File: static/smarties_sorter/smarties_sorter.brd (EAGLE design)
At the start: 170.2 x 100 mm, 17 parts, among them IC1 MEGA8-P, Q1 16Mhz, Q2 IRLZ44Z

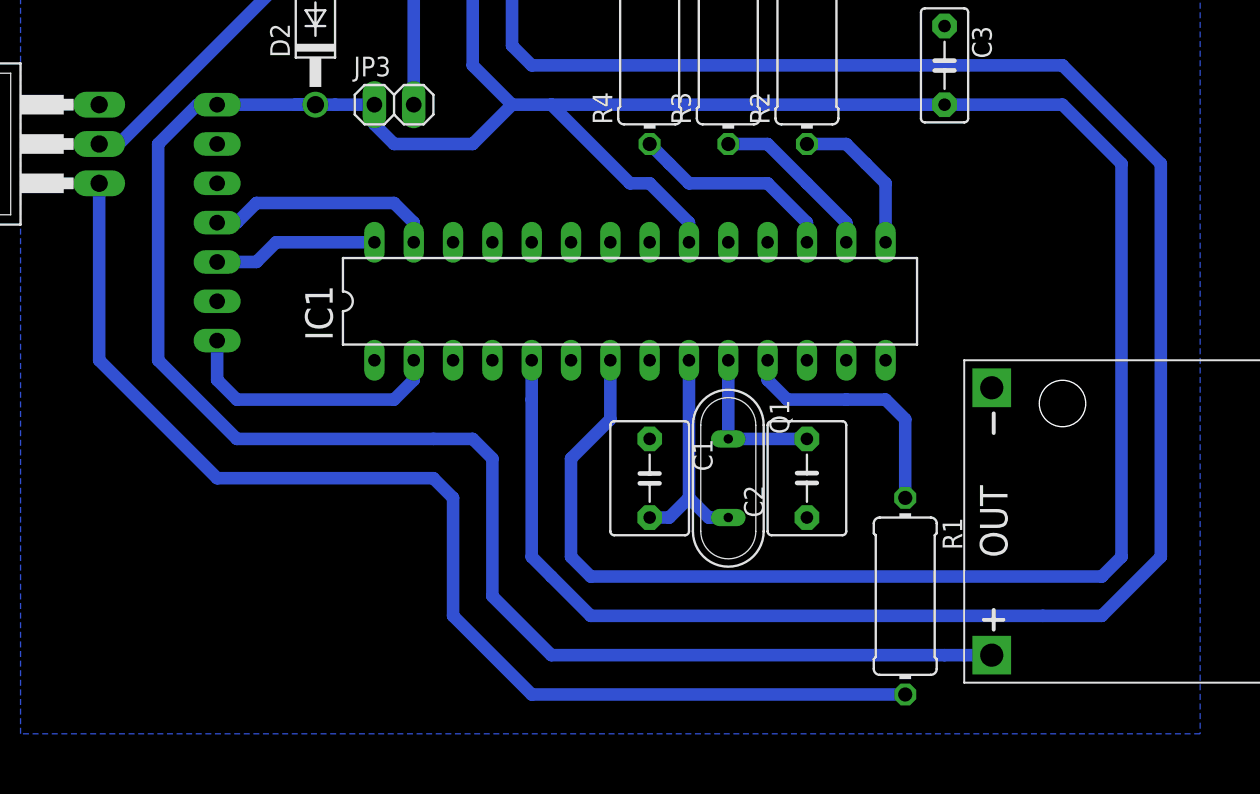
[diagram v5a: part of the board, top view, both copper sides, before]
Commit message: [Smarties_sorter] Change color sensor plug
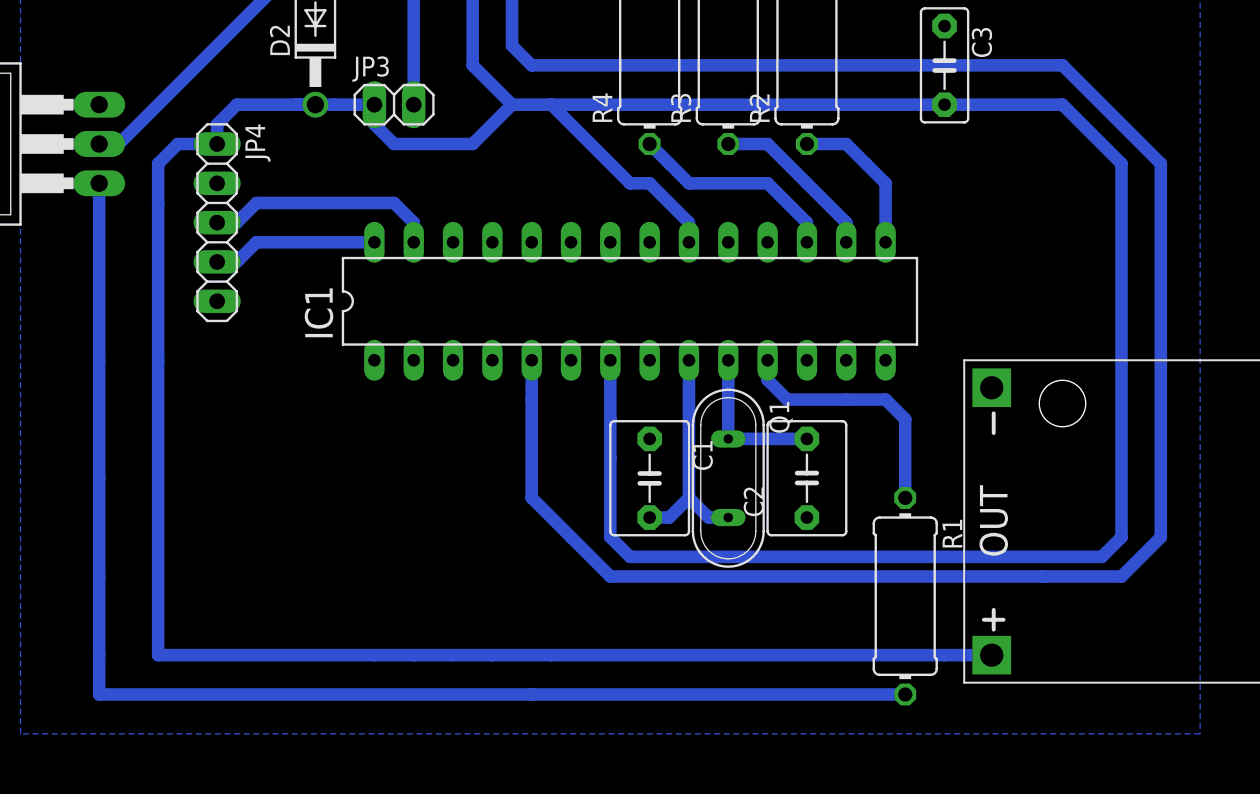
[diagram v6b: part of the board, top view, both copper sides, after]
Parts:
- JP4: device pinhead:1X07 -> pinhead:1X05
- flipped JP4 to the top
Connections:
- removed net N$15: IC1.2, JP4.7
- new net LED_CTRL: IC1.13, JP4.5
- net N$16: now also JP4.4; no longer JP4.5
- net N$17: now also JP4.3; no longer JP4.4
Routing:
- net N$15: track 17.6 -> 0.00 mm
- net N$8: track 76.9 -> 85.1 mm
- net N$6: track 135.9 -> 130.8 mm
- net 5V: track 254.0 -> 252.5 mm
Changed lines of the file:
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@@
 <element name="R3" library="resistor" package="0411/12" value="100" x="88.9" y="71.12" rot="R90"/>
 <element name="R4" library="resistor" package="0411/12" value="100" x="83.82" y="71.12" rot="R90"/>
-<element name="JP4" library="pinhead" package="1X07" value="" x="55.88" y="59.69" rot="MR270"/>
 <element name="D2" library="diode" package="DO41-10" value="1N4933" x="62.23" y="72.39" rot="R90"/>
 <element name="U$1" library="diy-modules" package="DC-DC-STEP-DOWN-LM2596" value="DC-DC-STEP-DOWN-LM2596" x="125.73" y="40.386" rot="R180"/>
@@
 </element>
 <element name="C3" library="capacitor-wima" package="C5B3" value="200nF" x="102.87" y="69.85" rot="R270"/>
+<element name="JP4" library="pinhead" package="1X05" value="" x="55.88" y="59.69" rot="R270"/>
 </elements>
 <signals>
@@
 <contactref element="Q2" pad="S"/>
 <contactref element="JP1" pad="4"/>
-<contactref element="JP4" pad="2"/>
 <wire x1="48.26" y1="67.31" x2="49.53" y2="67.31" width="0.8128" layer="16"/>
 <contactref element="U$1" pad="OUT-"/>
@@
 <contactref element="IC1" pad="22"/>
 <contactref element="C3" pad="1"/>
-<wire x1="49.53" y1="67.31" x2="55.88" y2="64.77" width="0" layer="19" extent="16-16"/>
+<contactref element="JP4" pad="2"/>
+<wire x1="49.53" y1="67.31" x2="55.88" y2="62.23" width="0" layer="19" extent="16-16"/>
 </signal>
 <signal name="N$1">
@@
 <contactref element="JP2" pad="2"/>
 <contactref element="JP3" pad="1"/>
-<contactref element="JP4" pad="1"/>
 <wire x1="72.39" y1="80.01" x2="72.39" y2="74.93" width="0.8128" layer="16"/>
 <wire x1="72.39" y1="64.77" x2="67.31" y2="64.77" width="0.8128" layer="16"/>
@@
 <wire x1="63.5" y1="67.31" x2="60.96" y2="67.31" width="0.8128" layer="16"/>
 <wire x1="60.96" y1="67.31" x2="62.23" y2="67.31" width="0.8128" layer="16"/>
-<wire x1="62.23" y1="67.31" x2="55.88" y2="67.31" width="0.8128" layer="16"/>
 <contactref element="D2" pad="C"/>
 <contactref element="U$1" pad="OUT+"/>
@@
 <wire x1="104.14" y1="31.75" x2="102.87" y2="31.75" width="0.8128" layer="16"/>
 <wire x1="102.87" y1="31.75" x2="77.47" y2="31.75" width="0.8128" layer="16"/>
-<wire x1="77.47" y1="31.75" x2="73.66" y2="35.56" width="0.8128" layer="16"/>
-<wire x1="73.66" y1="35.56" x2="73.66" y2="44.45" width="0.8128" layer="16"/>
-<wire x1="73.66" y1="44.45" x2="72.39" y2="45.72" width="0.8128" layer="16"/>
-<wire x1="72.39" y1="45.72" x2="69.85" y2="45.72" width="0.8128" layer="16"/>
-<wire x1="69.85" y1="45.72" x2="57.15" y2="45.72" width="0.8128" layer="16"/>
-<wire x1="57.15" y1="45.72" x2="52.07" y2="50.8" width="0.8128" layer="16"/>
-<wire x1="52.07" y1="50.8" x2="52.07" y2="64.77" width="0.8128" layer="16"/>
-<wire x1="52.07" y1="64.77" x2="54.61" y2="67.31" width="0.8128" layer="16"/>
-<wire x1="54.61" y1="67.31" x2="55.88" y2="67.31" width="0.8128" layer="16"/>
+<wire x1="77.47" y1="31.75" x2="73.66" y2="31.75" width="0.8128" layer="16"/>
+<wire x1="73.66" y1="31.75" x2="71.12" y2="31.75" width="0.8128" layer="16"/>
+<wire x1="71.12" y1="31.75" x2="68.58" y2="31.75" width="0.8128" layer="16"/>
+<wire x1="68.58" y1="31.75" x2="66.04" y2="31.75" width="0.8128" layer="16"/>
+<wire x1="66.04" y1="31.75" x2="52.07" y2="31.75" width="0.8128" layer="16"/>
+<wire x1="52.07" y1="31.75" x2="52.07" y2="50.8" width="0.8128" layer="16"/>
+<wire x1="52.07" y1="50.8" x2="52.07" y2="60.96" width="0.8128" layer="16"/>
+<wire x1="52.07" y1="60.96" x2="52.07" y2="63.5" width="0.8128" layer="16"/>
 <wire x1="81.28" y1="50.8" x2="81.28" y2="46.99" width="0.8128" layer="16"/>
-<wire x1="81.28" y1="46.99" x2="78.74" y2="44.45" width="0.8128" layer="16"/>
-<wire x1="78.74" y1="44.45" x2="78.74" y2="38.1" width="0.8128" layer="16"/>
-<wire x1="78.74" y1="38.1" x2="80.01" y2="36.83" width="0.8128" layer="16"/>
-<wire x1="80.01" y1="36.83" x2="113.03" y2="36.83" width="0.8128" layer="16"/>
-<wire x1="113.03" y1="36.83" x2="114.3" y2="38.1" width="0.8128" layer="16"/>
-<wire x1="114.3" y1="38.1" x2="114.3" y2="63.5" width="0.8128" layer="16"/>
+<wire x1="81.28" y1="46.99" x2="81.28" y2="44.45" width="0.8128" layer="16"/>
+<wire x1="81.28" y1="44.45" x2="81.28" y2="39.37" width="0.8128" layer="16"/>
+<wire x1="81.28" y1="39.37" x2="82.55" y2="38.1" width="0.8128" layer="16"/>
+<wire x1="82.55" y1="38.1" x2="113.03" y2="38.1" width="0.8128" layer="16"/>
+<wire x1="113.03" y1="38.1" x2="114.3" y2="39.37" width="0.8128" layer="16"/>
+<wire x1="114.3" y1="39.37" x2="114.3" y2="63.5" width="0.8128" layer="16"/>
 <wire x1="114.3" y1="63.5" x2="110.49" y2="67.31" width="0.8128" layer="16"/>
 <wire x1="110.49" y1="67.31" x2="77.47" y2="67.31" width="0.8128" layer="16"/>
@@
 <wire x1="82.55" y1="62.23" x2="77.47" y2="67.31" width="0.8128" layer="16"/>
 <contactref element="C3" pad="2"/>
+<contactref element="JP4" pad="1"/>
+<wire x1="52.07" y1="63.5" x2="53.34" y2="64.77" width="0.8128" layer="16"/>
+<wire x1="53.34" y1="64.77" x2="55.88" y2="64.77" width="0.8128" layer="16"/>
+<wire x1="55.88" y1="64.77" x2="55.88" y2="66.04" width="0.8128" layer="16"/>
+<wire x1="55.88" y1="66.04" x2="57.15" y2="67.31" width="0.8128" layer="16"/>
+<wire x1="57.15" y1="67.31" x2="60.96" y2="67.31" width="0.8128" layer="16"/>
 <wire x1="110.49" y1="67.31" x2="102.87" y2="67.31" width="0" layer="19" extent="16-16"/>
 </signal>
@@
 <wire x1="76.2" y1="69.85" x2="110.49" y2="69.85" width="0.8128" layer="16"/>
 <wire x1="110.49" y1="69.85" x2="116.84" y2="63.5" width="0.8128" layer="16"/>
-<wire x1="116.84" y1="63.5" x2="116.84" y2="38.1" width="0.8128" layer="16"/>
-<wire x1="116.84" y1="38.1" x2="113.03" y2="34.29" width="0.8128" layer="16"/>
-<wire x1="113.03" y1="34.29" x2="109.22" y2="34.29" width="0.8128" layer="16"/>
-<wire x1="109.22" y1="34.29" x2="80.01" y2="34.29" width="0.8128" layer="16"/>
-<wire x1="80.01" y1="34.29" x2="77.47" y2="36.83" width="0.8128" layer="16"/>
-<wire x1="77.47" y1="36.83" x2="76.2" y2="38.1" width="0.8128" layer="16"/>
-<wire x1="76.2" y1="38.1" x2="76.2" y2="48.26" width="0.8128" layer="16"/>
+<wire x1="116.84" y1="63.5" x2="116.84" y2="39.37" width="0.8128" layer="16"/>
+<wire x1="116.84" y1="39.37" x2="114.3" y2="36.83" width="0.8128" layer="16"/>
+<wire x1="114.3" y1="36.83" x2="109.22" y2="36.83" width="0.8128" layer="16"/>
+<wire x1="109.22" y1="36.83" x2="81.28" y2="36.83" width="0.8128" layer="16"/>
+<wire x1="81.28" y1="36.83" x2="78.74" y2="39.37" width="0.8128" layer="16"/>
+<wire x1="78.74" y1="39.37" x2="76.2" y2="41.91" width="0.8128" layer="16"/>
+<wire x1="76.2" y1="41.91" x2="76.2" y2="48.26" width="0.8128" layer="16"/>
 <wire x1="76.2" y1="48.26" x2="76.2" y2="50.8" width="0.8128" layer="16"/>
 </signal>
@@
 <contactref element="R1" pad="2"/>
 <wire x1="48.26" y1="62.23" x2="48.26" y2="50.8" width="0.8128" layer="16"/>
-<wire x1="48.26" y1="50.8" x2="55.88" y2="43.18" width="0.8128" layer="16"/>
-<wire x1="55.88" y1="43.18" x2="69.85" y2="43.18" width="0.8128" layer="16"/>
-<wire x1="69.85" y1="43.18" x2="71.12" y2="41.91" width="0.8128" layer="16"/>
-<wire x1="71.12" y1="41.91" x2="71.12" y2="34.29" width="0.8128" layer="16"/>
-<wire x1="71.12" y1="34.29" x2="76.2" y2="29.21" width="0.8128" layer="16"/>
+<wire x1="48.26" y1="50.8" x2="48.26" y2="43.18" width="0.8128" layer="16"/>
+<wire x1="48.26" y1="43.18" x2="48.26" y2="36.83" width="0.8128" layer="16"/>
+<wire x1="48.26" y1="36.83" x2="48.26" y2="31.75" width="0.8128" layer="16"/>
+<wire x1="48.26" y1="31.75" x2="48.26" y2="29.21" width="0.8128" layer="16"/>
+<wire x1="48.26" y1="29.21" x2="76.2" y2="29.21" width="0.8128" layer="16"/>
 <wire x1="76.2" y1="29.21" x2="100.33" y2="29.21" width="0.8128" layer="16"/>
 </signal>
@@
 <wire x1="83.82" y1="81.28" x2="83.82" y2="77.47" width="0.8128" layer="16"/>
 </signal>
-<signal name="N$15">
-<contactref element="JP4" pad="7"/>
-<contactref element="IC1" pad="2"/>
-<wire x1="55.88" y1="52.07" x2="55.88" y2="49.53" width="0.8128" layer="16"/>
-<wire x1="55.88" y1="49.53" x2="57.15" y2="48.26" width="0.8128" layer="16"/>
-<wire x1="57.15" y1="48.26" x2="67.31" y2="48.26" width="0.8128" layer="16"/>
-<wire x1="67.31" y1="48.26" x2="68.58" y2="49.53" width="0.8128" layer="16"/>
-<wire x1="68.58" y1="49.53" x2="68.58" y2="50.8" width="0.8128" layer="16"/>
-</signal>
 <signal name="N$16">
-<contactref element="JP4" pad="5"/>
 <contactref element="IC1" pad="28"/>
-<wire x1="66.04" y1="58.42" x2="59.69" y2="58.42" width="0.8128" layer="16"/>
-<wire x1="59.69" y1="58.42" x2="58.42" y2="57.15" width="0.8128" layer="16"/>
-<wire x1="58.42" y1="57.15" x2="55.88" y2="57.15" width="0.8128" layer="16"/>
+<contactref element="JP4" pad="4"/>
+<wire x1="55.88" y1="57.15" x2="57.15" y2="57.15" width="0.8128" layer="16"/>
+<wire x1="57.15" y1="57.15" x2="58.42" y2="58.42" width="0.8128" layer="16"/>
+<wire x1="58.42" y1="58.42" x2="66.04" y2="58.42" width="0.8128" layer="16"/>
 </signal>
 <signal name="N$17">
-<contactref element="JP4" pad="4"/>
 <contactref element="IC1" pad="27"/>
+<contactref element="JP4" pad="3"/>
 <wire x1="55.88" y1="59.69" x2="57.15" y2="59.69" width="0.8128" layer="16"/>
 <wire x1="57.15" y1="59.69" x2="58.42" y2="60.96" width="0.8128" layer="16"/>
@@
 <wire x1="153.63" y1="43.18" x2="153.67" y2="43.14" width="0.8128" layer="16"/>
 </signal>
+<signal name="LED_CTRL">
+<contactref element="IC1" pad="13"/>
+<contactref element="JP4" pad="5"/>
+<wire x1="55.88" y1="54.61" x2="96.52" y2="50.8" width="0" layer="19" extent="1-1"/>
+</signal>
 </signals>

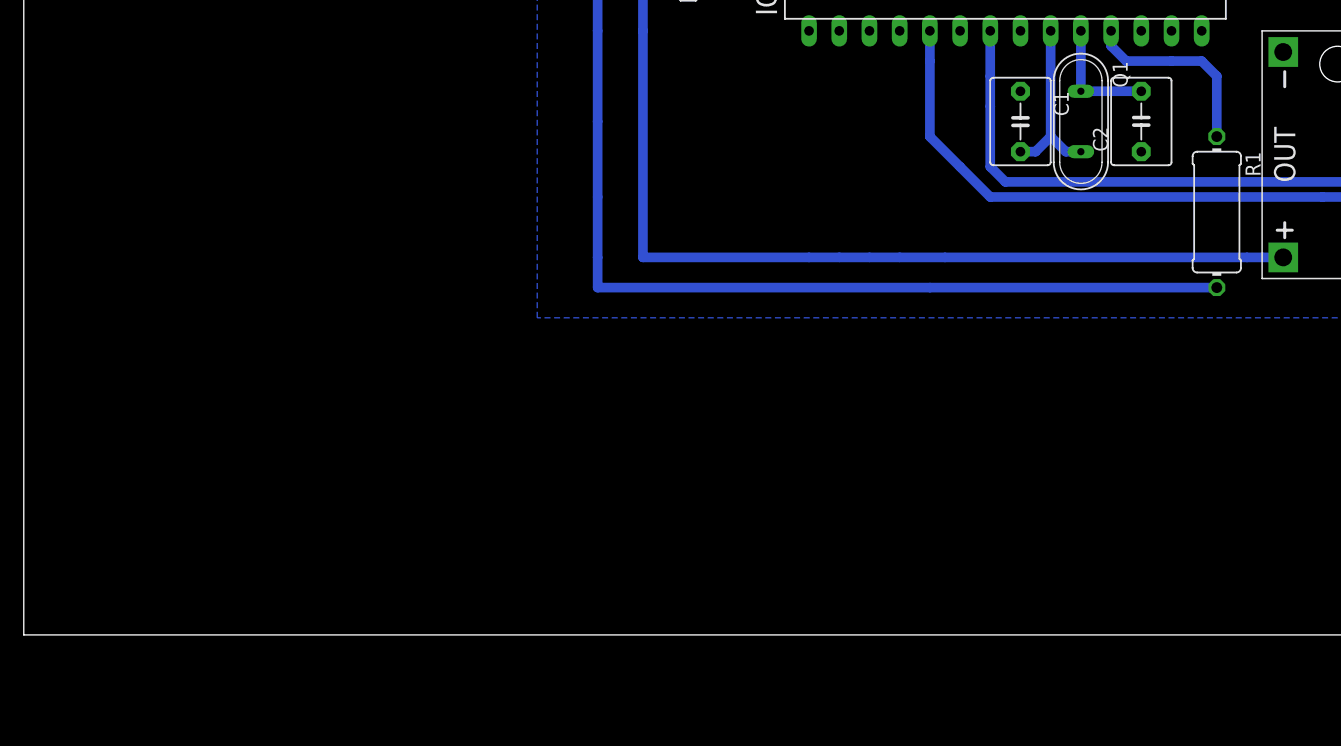
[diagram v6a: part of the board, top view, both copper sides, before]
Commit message: [Smarties_sorter] Adds resistor to pull down motor command
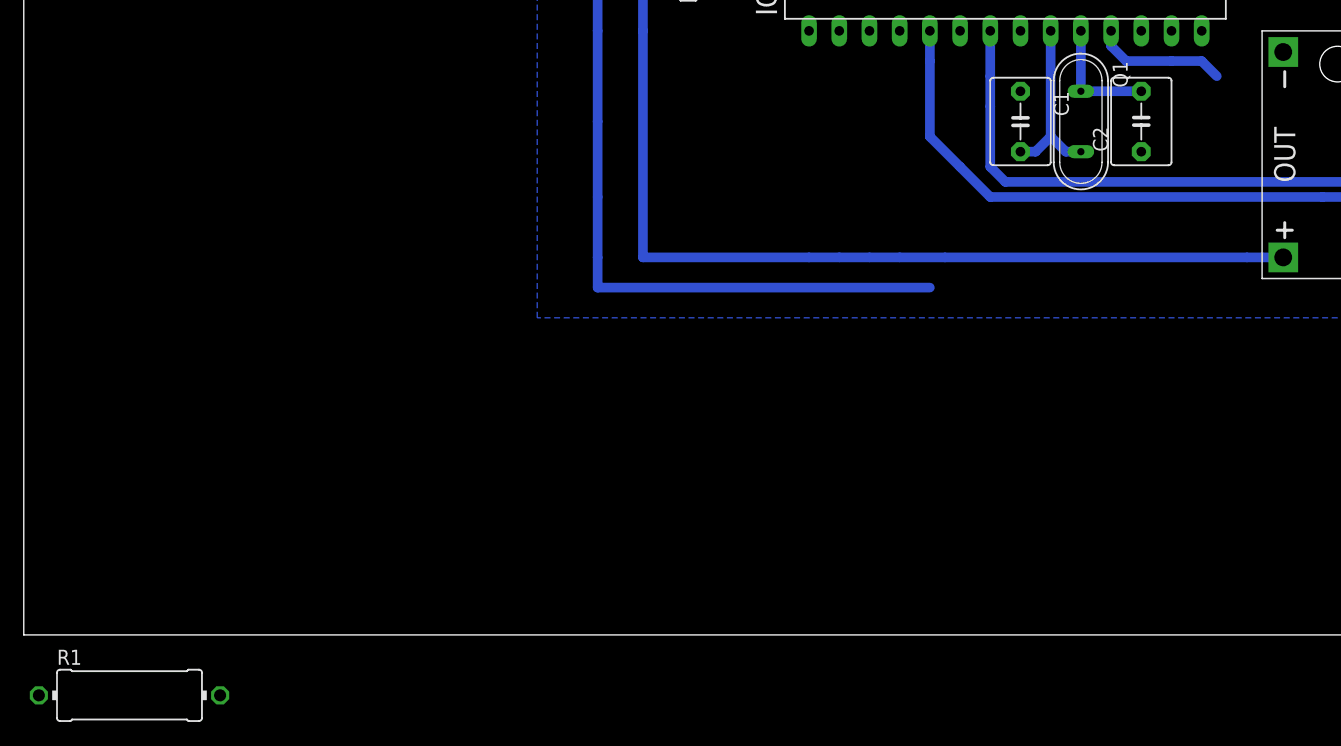
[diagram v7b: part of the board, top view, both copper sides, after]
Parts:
- R1: value 1k -> 10Kohms; device resistor:0411/12 -> rcl:0414/15
- moved R1 100.1 mm to (8.89, -5.08), turned to 0 degrees
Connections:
- removed net N$8: Q2.G, R1.2
- net GND: now also R1.2
- net N$9: now also Q2.G
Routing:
- net N$8: track 85.1 -> 0.00 mm
- net N$9: track 16.3 -> 72.2 mm
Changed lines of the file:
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@@
 <element name="Q2" library="transistor-power" package="TO220BH" value="IRLZ44Z" x="41.91" y="64.77" rot="R90"/>
 <element name="JP3" library="pinhead" package="1X02" value="" x="67.31" y="67.31"/>
-<element name="R1" library="resistor" package="0411/12" value="1k" x="100.33" y="35.56" rot="R270"/>
 <element name="R2" library="resistor" package="0411/12" value="180" x="93.98" y="71.12" rot="R90"/>
 <element name="R3" library="resistor" package="0411/12" value="100" x="88.9" y="71.12" rot="R90"/>
@@
 <element name="C3" library="capacitor-wima" package="C5B3" value="200nF" x="102.87" y="69.85" rot="R270"/>
 <element name="JP4" library="pinhead" package="1X05" value="" x="55.88" y="59.69" rot="R270"/>
+<element name="R1" library="rcl" package="0414/15" value="10Kohms" x="8.89" y="-5.08"/>
 </elements>
 <signals>
@@
 <contactref element="C3" pad="1"/>
 <contactref element="JP4" pad="2"/>
+<contactref element="R1" pad="2"/>
+<wire x1="55.88" y1="62.23" x2="16.51" y2="-5.08" width="0" layer="19" extent="1-1"/>
 <wire x1="49.53" y1="67.31" x2="55.88" y2="62.23" width="0" layer="19" extent="16-16"/>
+<wire x1="81.28" y1="58.42" x2="81.28" y2="81.28" width="0" layer="19" extent="1-1"/>
 </signal>
 <signal name="N$1">
@@
 <contactref element="D2" pad="A"/>
 </signal>
-<signal name="N$8">
+<signal name="N$9">
+<contactref element="IC1" pad="11"/>
+<wire x1="91.44" y1="50.8" x2="91.44" y2="49.53" width="0.8128" layer="16"/>
+<wire x1="91.44" y1="49.53" x2="92.71" y2="48.26" width="0.8128" layer="16"/>
+<wire x1="92.71" y1="48.26" x2="96.52" y2="48.26" width="0.8128" layer="16"/>
+<wire x1="96.52" y1="48.26" x2="99.06" y2="48.26" width="0.8128" layer="16"/>
+<wire x1="99.06" y1="48.26" x2="100.33" y2="46.99" width="0.8128" layer="16"/>
 <contactref element="Q2" pad="G"/>
-<contactref element="R1" pad="2"/>
 <wire x1="48.26" y1="62.23" x2="48.26" y2="50.8" width="0.8128" layer="16"/>
 <wire x1="48.26" y1="50.8" x2="48.26" y2="43.18" width="0.8128" layer="16"/>
@@
 <wire x1="48.26" y1="31.75" x2="48.26" y2="29.21" width="0.8128" layer="16"/>
 <wire x1="48.26" y1="29.21" x2="76.2" y2="29.21" width="0.8128" layer="16"/>
-<wire x1="76.2" y1="29.21" x2="100.33" y2="29.21" width="0.8128" layer="16"/>
-</signal>
-<signal name="N$9">
 <contactref element="R1" pad="1"/>
-<contactref element="IC1" pad="11"/>
-<wire x1="91.44" y1="50.8" x2="91.44" y2="49.53" width="0.8128" layer="16"/>
-<wire x1="91.44" y1="49.53" x2="92.71" y2="48.26" width="0.8128" layer="16"/>
-<wire x1="92.71" y1="48.26" x2="96.52" y2="48.26" width="0.8128" layer="16"/>
-<wire x1="96.52" y1="48.26" x2="99.06" y2="48.26" width="0.8128" layer="16"/>
-<wire x1="99.06" y1="48.26" x2="100.33" y2="46.99" width="0.8128" layer="16"/>
-<wire x1="100.33" y1="46.99" x2="100.33" y2="41.91" width="0.8128" layer="16"/>
+<wire x1="76.2" y1="29.21" x2="92.71" y2="48.26" width="0" layer="19" extent="16-16"/>
+<wire x1="1.27" y1="-5.08" x2="48.26" y2="29.21" width="0" layer="19" extent="16-16"/>
 </signal>
 <signal name="N$3">
